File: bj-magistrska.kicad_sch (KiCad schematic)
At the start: 3 parts, among them J1 Screw_Terminal_01x02, J2 20 pos, J3 Screw_Terminal_01x02

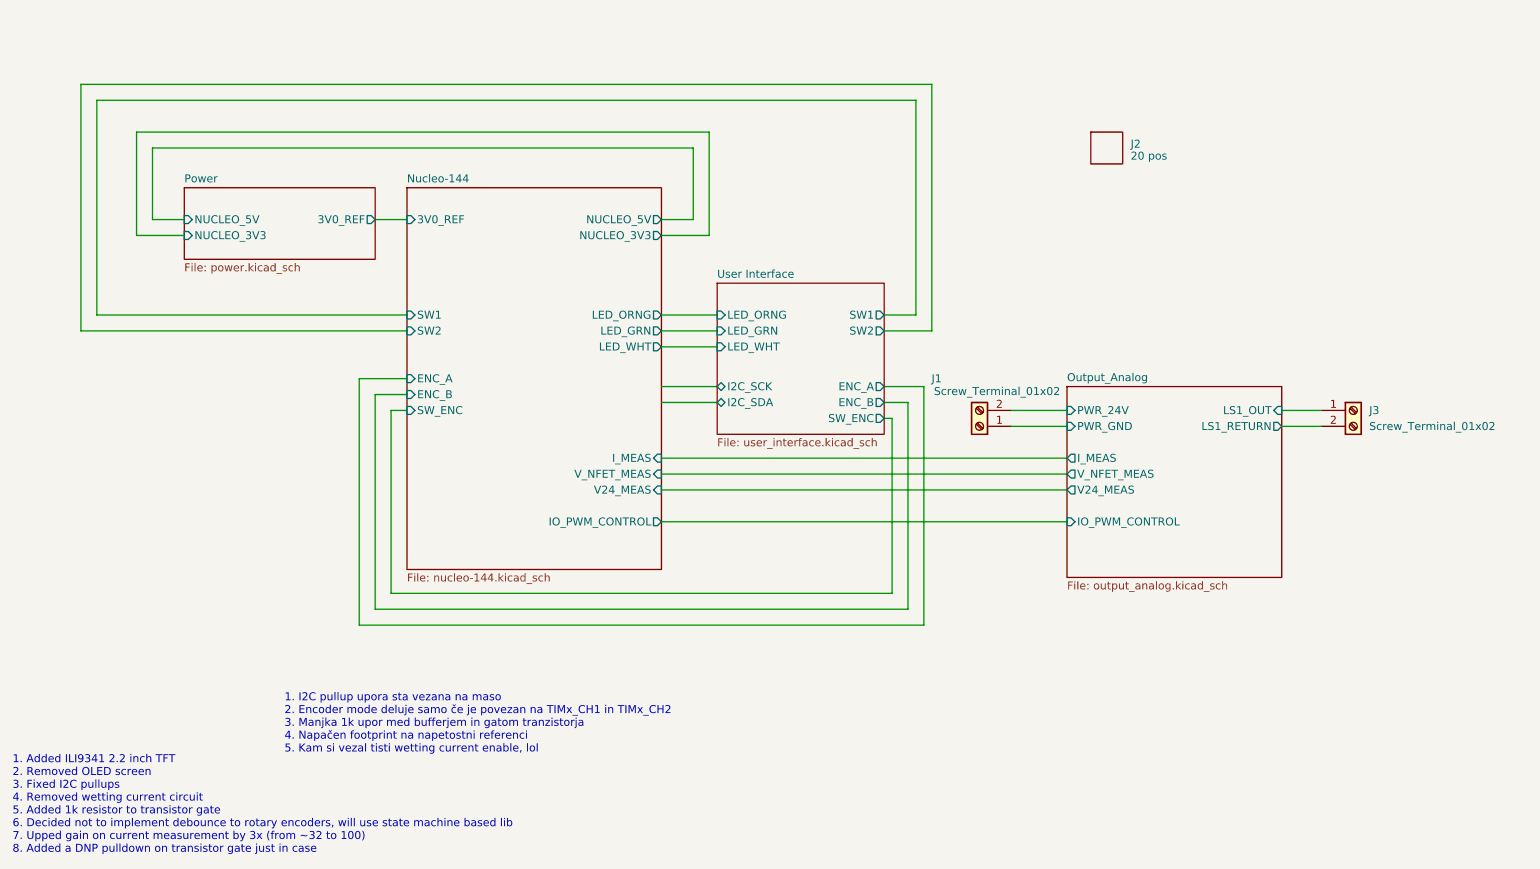
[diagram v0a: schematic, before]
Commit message: Cleaned up unecessary HMI, optimized sheets.
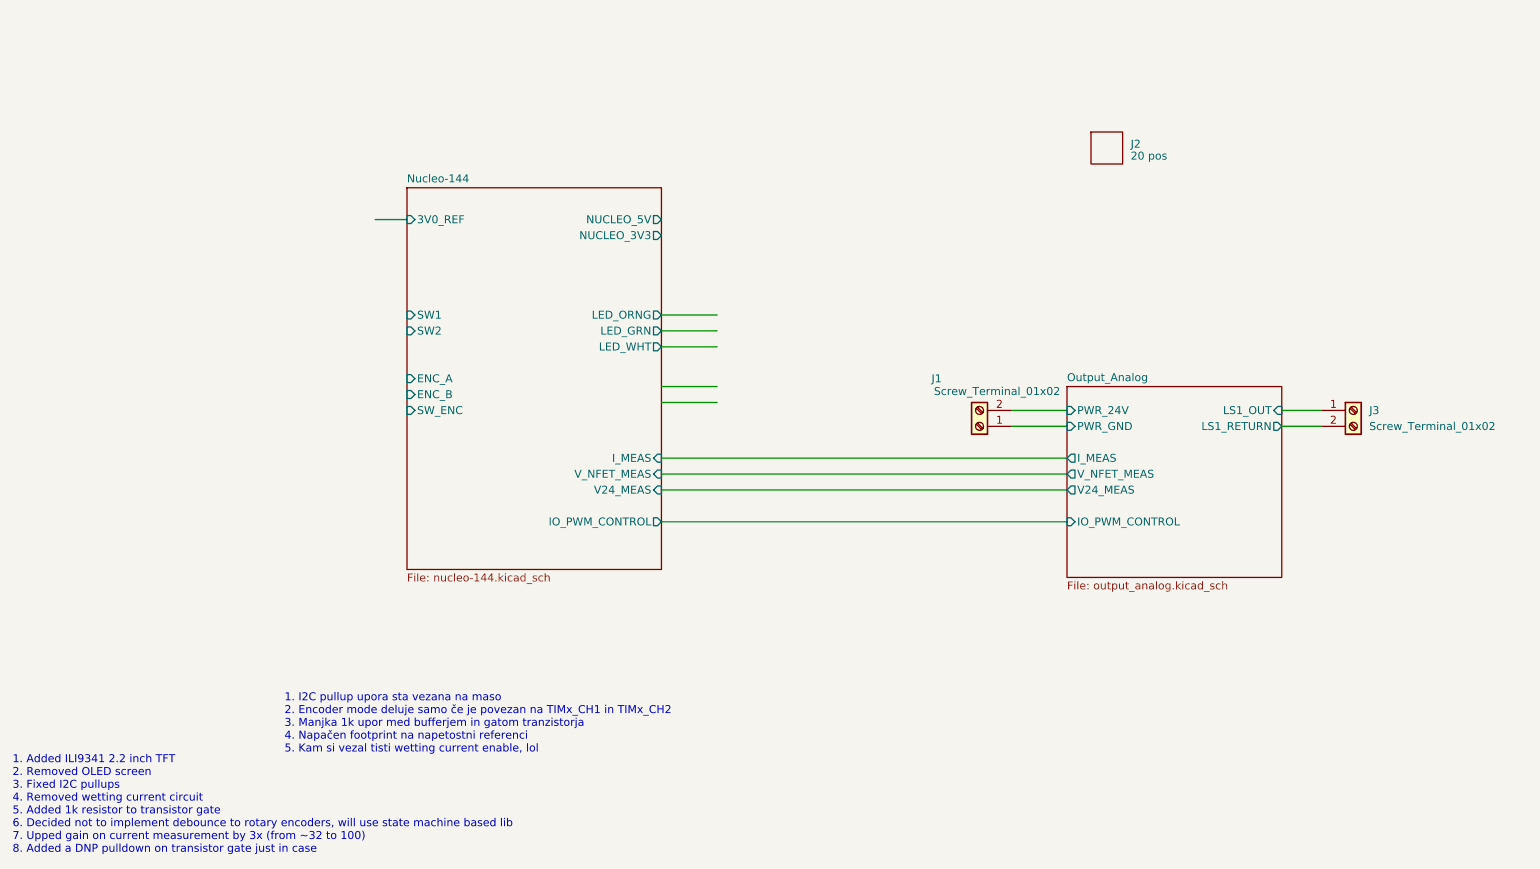
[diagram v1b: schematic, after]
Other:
- removed sheet Power
- removed sheet User Interface
- title: (none) -> Procyon [Capstone]

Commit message: Added HS current sense to analog chain. Refactored schematics. Added snubber to the n-fet. Moved some stuff to DNP for clarity.
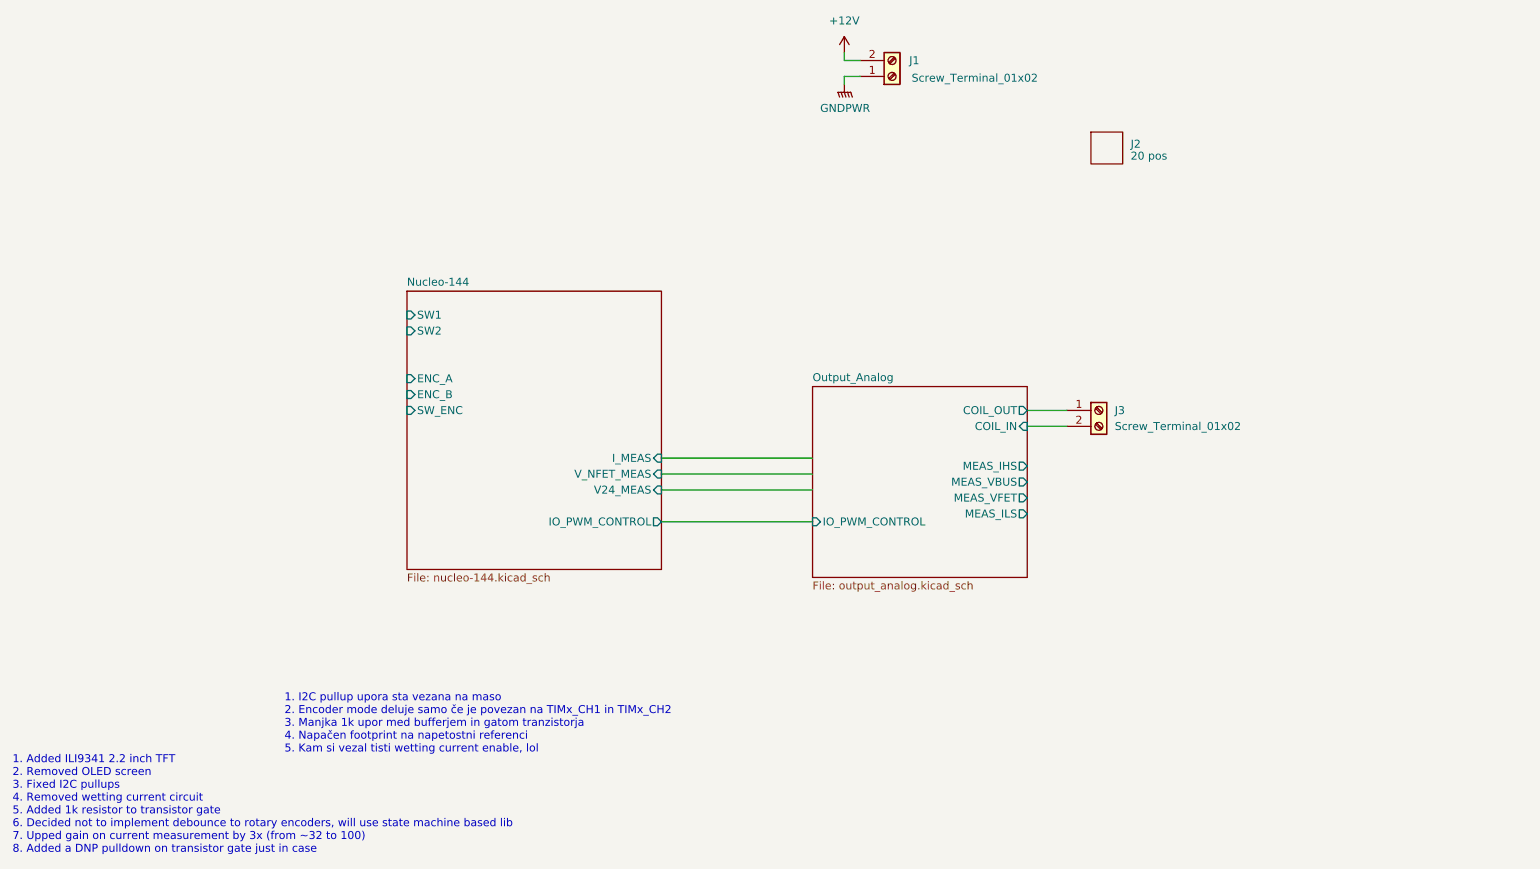
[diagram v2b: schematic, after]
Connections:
- net Output_Analog/LS1_OUT renamed Output_Analog/COIL_OUT
- net Output_Analog/LS1_RETURN renamed Output_Analog/COIL_IN
- net Output_Analog/PWR_24V renamed +12V
- net Output_Analog/PWR_GND renamed GNDPWR
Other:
- sheet Nucleo-144 ports: added none; removed 3V0_REF, LED_GRN, LED_ORNG, LED_WHT, NUCLEO_3V3, NUCLEO_5V
- sheet Output_Analog ports: added COIL_IN, COIL_OUT, MEAS_IHS, MEAS_ILS, MEAS_VBUS, MEAS_VFET; removed I_MEAS, LS1_OUT, LS1_RETURN, PWR_24V, PWR_GND, V24_MEAS, V_NFET_MEAS
- moved on the sheet: J1, J3

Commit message: Refactored Nucleo sheet. Added back my library. Started minor work on the PCB.
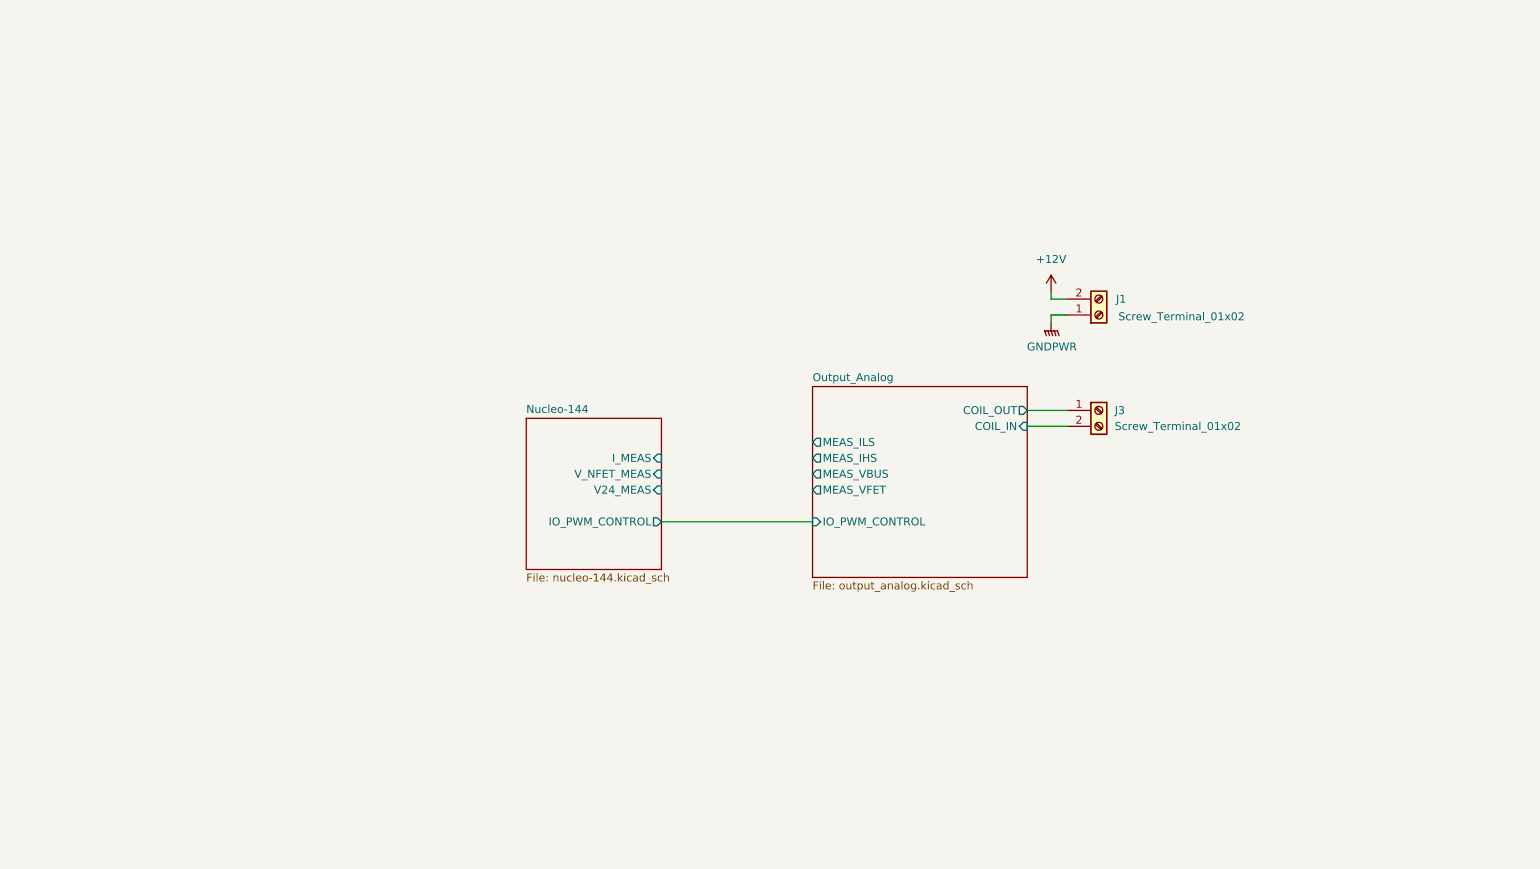
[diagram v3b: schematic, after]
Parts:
- removed J2: 20 pos, symbol athanniss-lib:DUMMY_HEADER
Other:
- sheet Nucleo-144 ports: added none; removed ENC_A, ENC_B, SW1, SW2, SW_ENC
- note removed: "1. Added ILI9341 2.2 inch TFT 2. Removed OLED screen 3. Fixed I2C pullups 4. Removed wetting current circuit 5. Added 1k resistor to transistor gate 6. Decided not to implement debounce to rotary encoders, will use state machine based lib 7. Upped gain on current measurement by 3x (from ~32 to 100) 8. Added a DNP pulldown on transistor gate just in case"
- note removed: "1. I2C pullup upora sta vezana na maso 2. Encoder mode deluje samo če je povezan na TIMx_CH1 in TIMx_CH2 3. Manjka 1k upor med bufferjem in gatom tranzistorja 4. Napačen footprint na napetostni referenci 5. Kam si vezal tisti wetting current enable, lol"
- moved on the sheet: J1

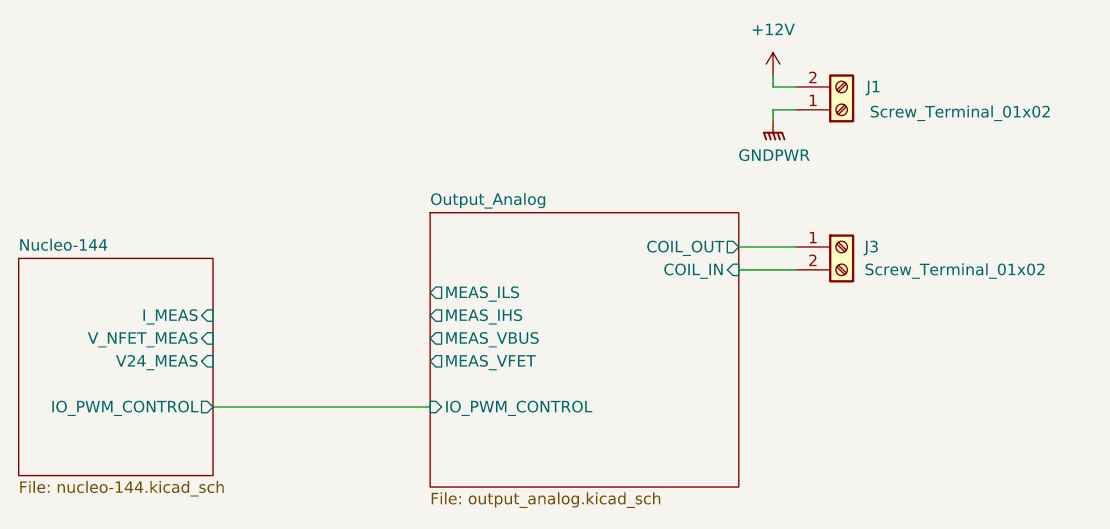
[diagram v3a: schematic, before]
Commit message: Finalized V1.1. Refactor schematics (PCB is ripped up) for HS measurement. Kept LS custom chain for reference.
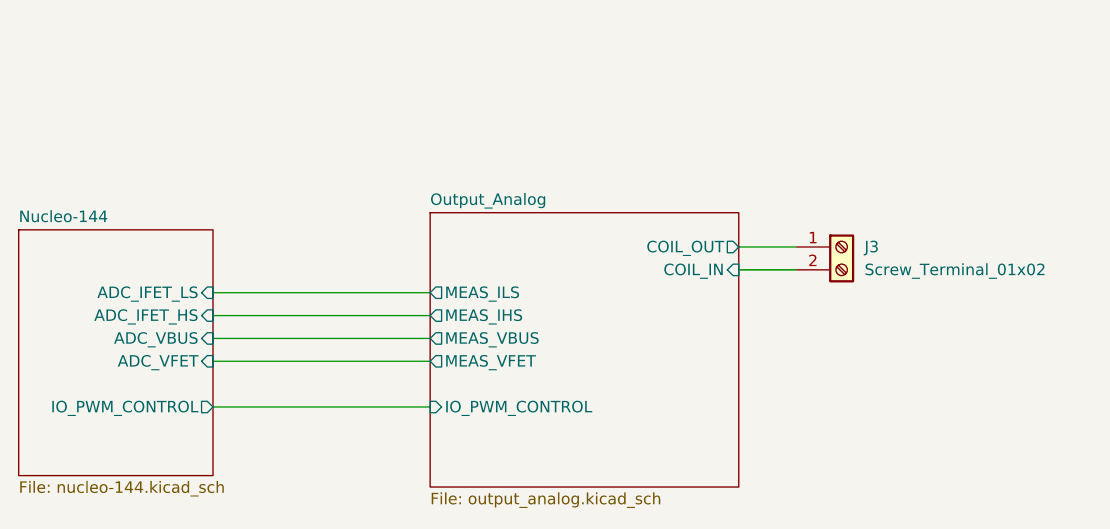
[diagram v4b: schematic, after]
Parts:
- removed J1: Screw_Terminal_01x02, TerminalBlock_Phoenix:TerminalBlock_Phoenix_MKDS-1,5-2-5.08_1x02_P5.08mm_Horizontal, symbol Connector:Screw_Terminal_01x02
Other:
- sheet Nucleo-144 ports: added ADC_IFET_HS, ADC_IFET_LS, ADC_VBUS, ADC_VFET; removed I_MEAS, V24_MEAS, V_NFET_MEAS
